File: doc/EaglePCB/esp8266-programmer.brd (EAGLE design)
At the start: 101.3 x 82.5 mm, 6 parts

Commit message: small fixes
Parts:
- R1, R2: value 10k -> 1k
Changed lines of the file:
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@@
 <elements>
 <element name="PRG" library="SparkFun-Retired" package="TACTILE-PTH" value="" x="17.78" y="64.77" rot="R180"/>
-<element name="R1" library="eagle-ltspice" package="0207/10" value="10k" x="41.91" y="58.42">
+<element name="R1" library="eagle-ltspice" package="0207/10" value="1k" x="41.91" y="58.42">
 <attribute name="SPICEMODEL" value="NONE" x="41.91" y="58.42" size="1.778" layer="27" display="off"/>
 <attribute name="SPICEPREFIX" value="R" x="41.91" y="58.42" size="1.778" layer="27" display="off"/>
 </element>
-<element name="R2" library="eagle-ltspice" package="0207/10" value="10k" x="52.07" y="68.58" rot="R180">
+<element name="R2" library="eagle-ltspice" package="0207/10" value="1k" x="52.07" y="68.58" rot="R180">
 <attribute name="SPICEMODEL" value="NONE" x="52.07" y="68.58" size="1.778" layer="27" rot="R180" display="off"/>
 <attribute name="SPICEPREFIX" value="R" x="52.07" y="68.58" size="1.778" layer="27" rot="R180" display="off"/>

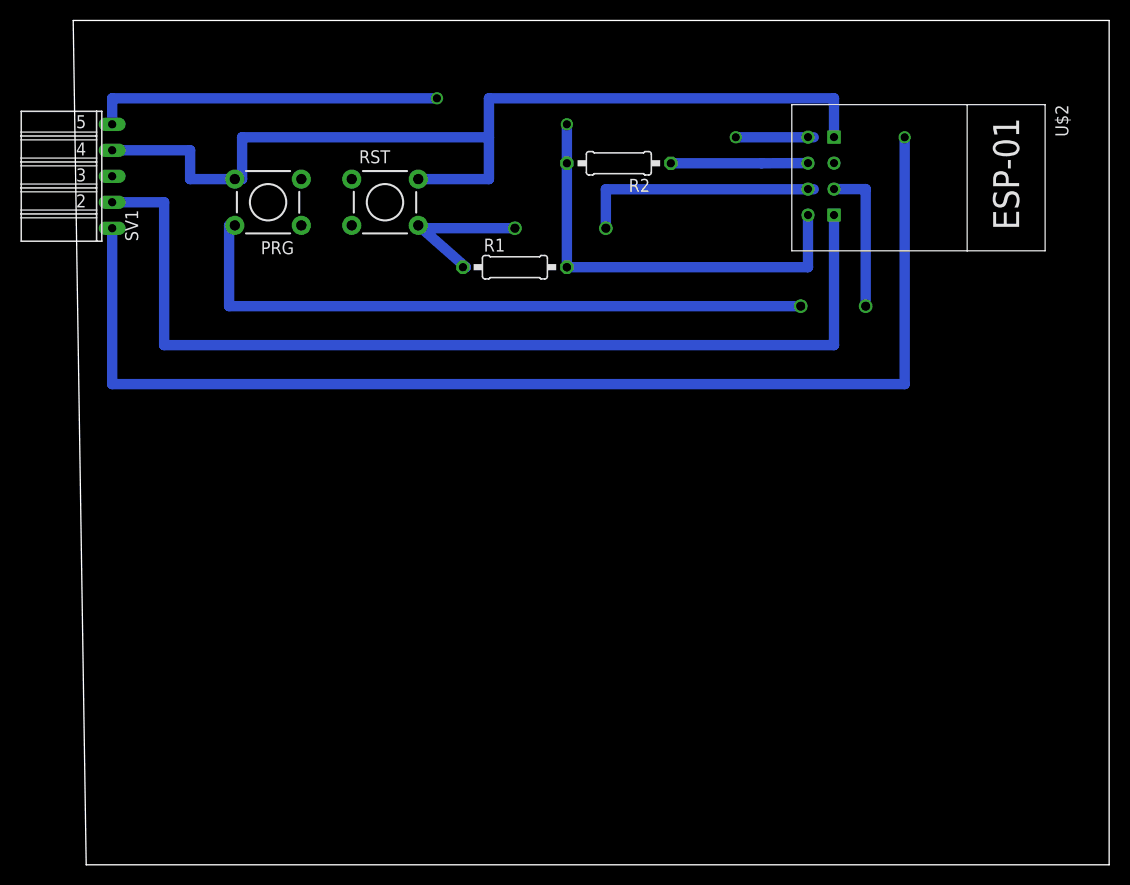
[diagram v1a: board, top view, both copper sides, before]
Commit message: correct PCB design and add PIR IoT device
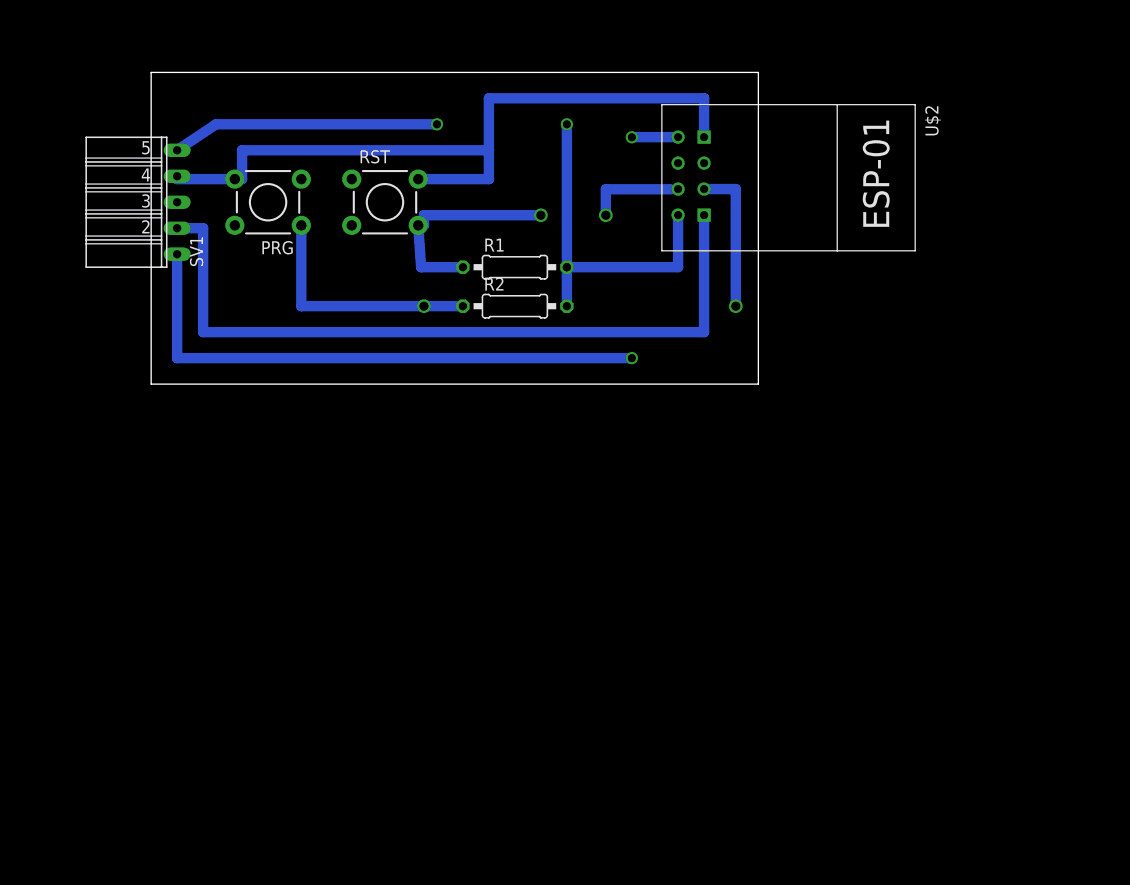
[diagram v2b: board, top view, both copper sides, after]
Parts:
- R1, R2: value 1k -> 5k
- moved R2 17.3 mm to (41.9, 54.6), turned to 0 degrees
- moved U$2 12.7 mm to (66.0, 67.3)
- moved SV1 6.84 mm to (8.89, 64.8)
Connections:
- removed net CH_PD: R2.1, U$2.CH_PD
- net GPIO0: now also PRG.1, R2.1; no longer PRG.2
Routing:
- net RX-TX: track 124.5 -> 59.1 mm
- net GPIO0: track 78.9 -> 38.2 mm
- net TX-RX: track 97.2 -> 73.1 mm
- net GND: track 96.1 -> 73.2 mm
- net 3V3: track 76.9 -> 59.9 mm
- net CH_PD: track 13.4 -> 0.00 mm
- net RST: track 39.5 -> 30.1 mm
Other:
- board size 101.3 x 82.5 mm -> 59.4 x 30.5 mm
